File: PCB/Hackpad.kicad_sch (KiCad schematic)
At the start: 11 parts, among them SW1 SW_Push, SW2 SW_Push, SW3 SW_Push, SW4 SW_Push, SW5 RotaryEncoder, U1 XIAO-RP2040-DIP, U2 SSD1306

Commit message: Connected the OLED to 3.3V instead of 5V
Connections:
- net +5V: no longer U2.1 (VCC)
- net +3.3V: now reaches U1.12 (3V3)
- net +3.3V: now also U2.1 (VCC)
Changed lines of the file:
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@@
+	)
+	(symbol
+		(lib_id "power:+3.3V")
+		(at 180.34 92.71 90)
+		(unit 1)
+		(exclude_from_sim no)
+		(in_bom yes)
+		(on_board yes)
+		(dnp no)
+		(fields_autoplaced yes)
+		(property "Reference" "#PWR02"
+			(at 184.15 92.71 0)
+			(effects
+				(font
+					(size 1.27 1.27)
+				)
+				(hide yes)
+			)
+		)
+		(property "Value" "+3.3V"
+			(at 176.53 92.7099 90)
+			(effects
+				(font
+					(size 1.27 1.27)
+				)
+				(justify left)
+			)
+		)
+		(property "Footprint" ""
+			(at 180.34 92.71 0)
+			(effects
+				(font
+					(size 1.27 1.27)
+				)
+				(hide yes)
+			)
+		)
+		(property "Datasheet" ""
+			(at 180.34 92.71 0)
+			(effects
+				(font
+					(size 1.27 1.27)
+				)
+				(hide yes)
+			)
+		)
+		(property "Description" "Power symbol creates a global label with name \"+3.3V\""
+			(at 180.34 92.71 0)
+			(effects
+				(font
+					(size 1.27 1.27)
+				)
+				(hide yes)
+			)
+		)
+		(pin "1"
+		)
+		(instances
+			(project ""
+				(path "/57562cda-4c79-470d-93dd-be91ac0b72c0"
+					(reference "#PWR02")
+					(unit 1)
+				)
+			)
+		)
 	)
 	(symbol
@@
 	)
 	(symbol
+		(lib_id "power:+3.3V")
+		(at 161.29 95.25 270)
+		(unit 1)
+		(exclude_from_sim no)
+		(in_bom yes)
+		(on_board yes)
+		(dnp no)
+		(fields_autoplaced yes)
+		(property "Reference" "#PWR09"
+			(at 157.48 95.25 0)
+			(effects
+				(font
+					(size 1.27 1.27)
+				)
+				(hide yes)
+			)
+		)
+		(property "Value" "+3.3V"
+			(at 165.1 95.2499 90)
+			(effects
+				(font
+					(size 1.27 1.27)
+				)
+				(justify left)
+			)
+		)
+		(property "Footprint" ""
+			(at 161.29 95.25 0)
+			(effects
+				(font
+					(size 1.27 1.27)
+				)
+				(hide yes)
+			)
+		)
+		(property "Datasheet" ""
+			(at 161.29 95.25 0)
+			(effects
+				(font
+					(size 1.27 1.27)
+				)
+				(hide yes)
+			)
+		)
+		(property "Description" "Power symbol creates a global label with name \"+3.3V\""
+			(at 161.29 95.25 0)
+			(effects
+				(font
+					(size 1.27 1.27)
+				)
+				(hide yes)
+			)
+		)
+		(pin "1"
+		)
+		(instances
+			(project ""
+				(path "/57562cda-4c79-470d-93dd-be91ac0b72c0"
+					(reference "#PWR09")
+					(unit 1)
+				)
+			)
+		)
+	)
+	(symbol
 		(lib_id "power:GND")
 		(at 180.34 95.25 270)
@@
 					(unit 1)
 				)
-			)
-		)
-	)
-	(symbol
-		(lib_id "power:+5V")
-		(at 180.34 92.71 90)
-		(unit 1)
-		(exclude_from_sim no)
-		(in_bom yes)
-		(on_board yes)
-		(dnp no)
-		(fields_autoplaced yes)
-		(property "Reference" "#PWR02"
-			(at 184.15 92.71 0)
-			(effects
-				(font
-					(size 1.27 1.27)
-				)
-				(hide yes)
-			)
-		)
-		(property "Value" "+5V"
-			(at 176.53 92.7099 90)
-			(effects
-				(font
-					(size 1.27 1.27)
-				)
-				(justify left)
-			)
-		)
-		(property "Footprint" ""
-			(at 180.34 92.71 0)
-			(effects
-				(font
-					(size 1.27 1.27)
-				)
-				(hide yes)
-			)
-		)
-		(property "Datasheet" ""
-			(at 180.34 92.71 0)
-			(effects
-				(font
-					(size 1.27 1.27)
-				)
-				(hide yes)
-			)
-		)
-		(property "Description" "Power symbol creates a global label with name \"+5V\""
-			(at 180.34 92.71 0)
-			(effects
-				(font
-					(size 1.27 1.27)
-				)
-				(hide yes)
-			)
-		)
-		(pin "1"
-		)
-		(instances
-			(project ""
-				(path "/57562cda-4c79-470d-93dd-be91ac0b72c0"
-					(reference "#PWR02")
-					(unit 1)
-				)

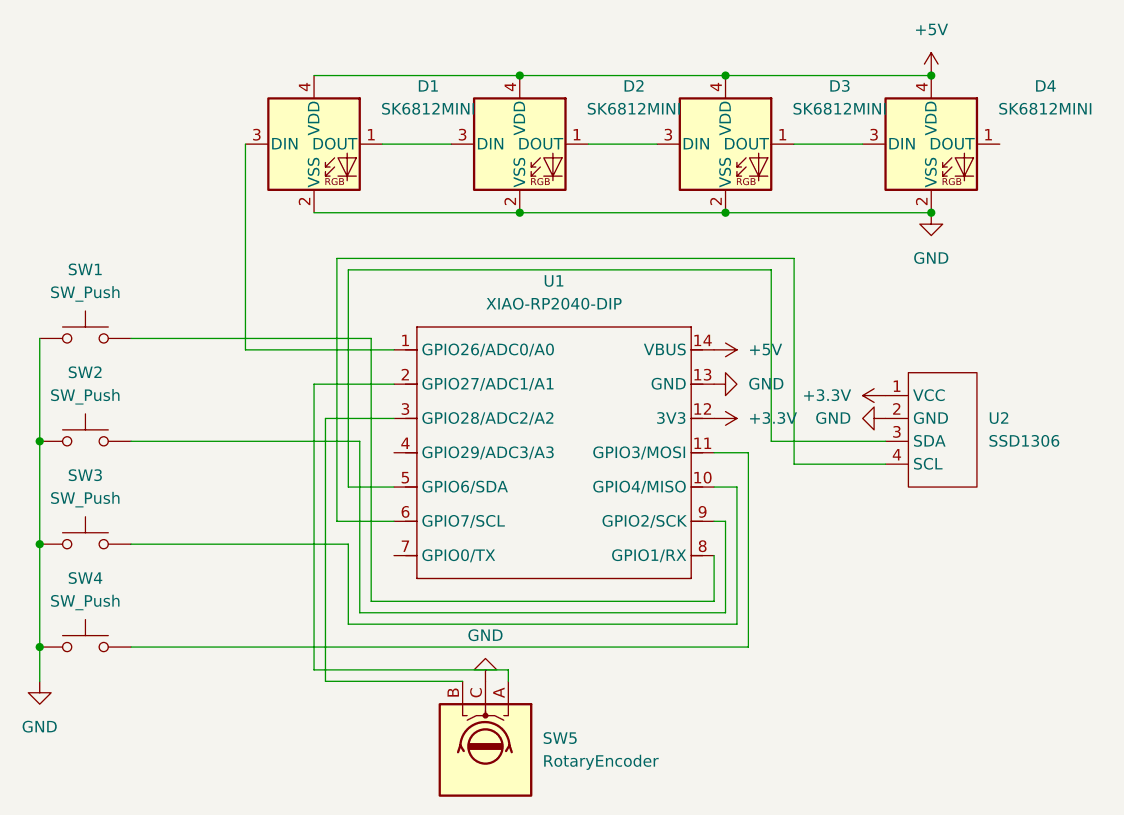
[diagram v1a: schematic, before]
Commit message: Rearranged pins on the OLED
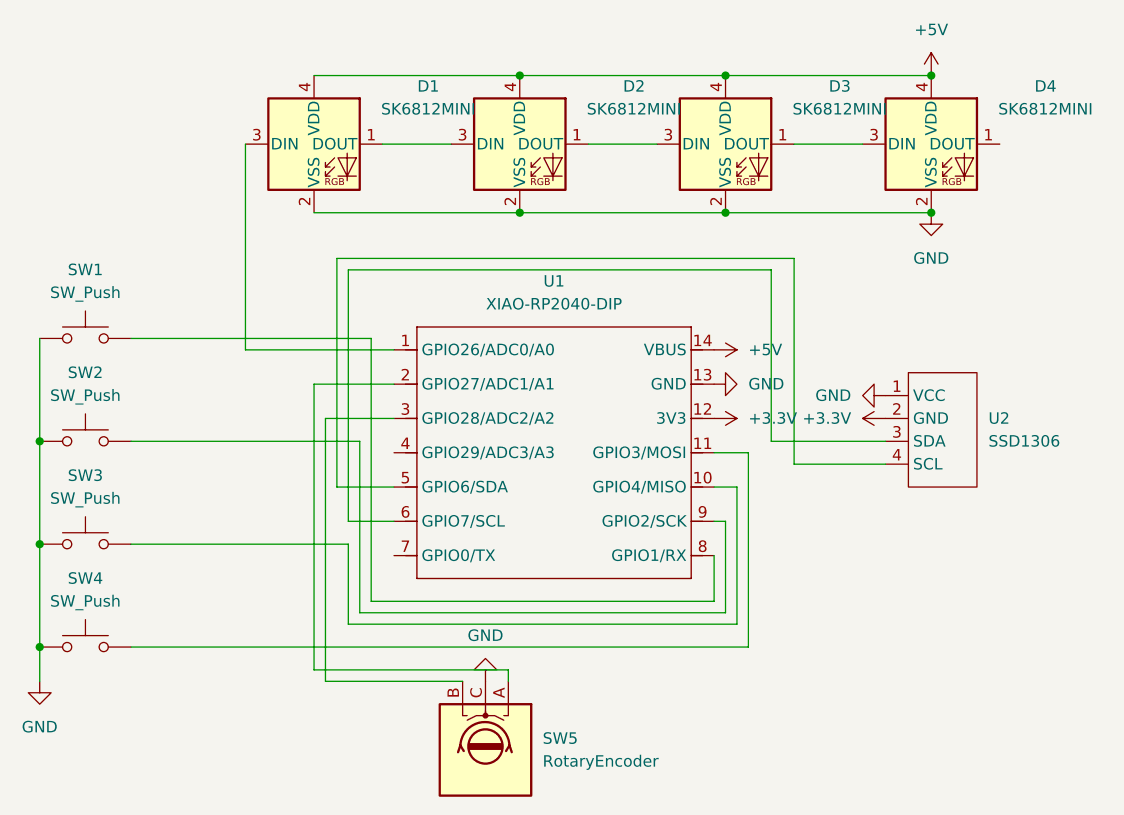
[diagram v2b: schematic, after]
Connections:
- net +3.3V: now also U2.2 (GND); no longer U2.1 (VCC)
- net GND: now also U2.1 (VCC); no longer U2.2 (GND)
- net at U1.5 (GPIO6/SDA): now also U2.4 (SCL); no longer U2.3 (SDA)
- net at U1.6 (GPIO7/SCL): now also U2.3 (SDA); no longer U2.4 (SCL)
